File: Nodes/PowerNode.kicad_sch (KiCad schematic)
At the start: 12 parts, among them T1 Conn_01x01, U1 STM32G431KBT6, Y1 SG-8018CE_8.0000M-TJHPA3

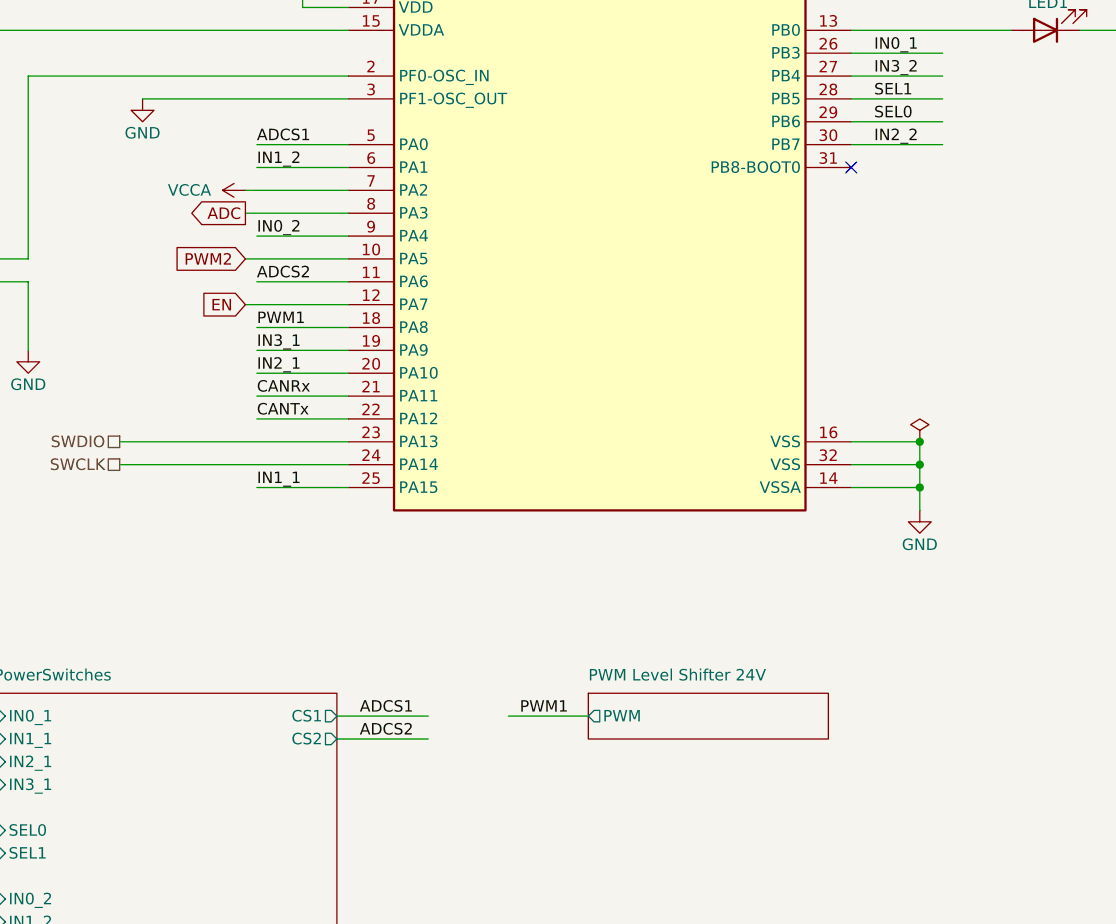
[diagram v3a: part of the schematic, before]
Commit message: Nodes v2.2.3
- Added one more PWM Level shifter
- Controllable amplitude of PWM by switches
- Added labels
- Added resistors to solve BOOT issue
- I2C1 pins changed
- More GND vias
- Higher resistance for adjustable voltage regulators
- Other small changes
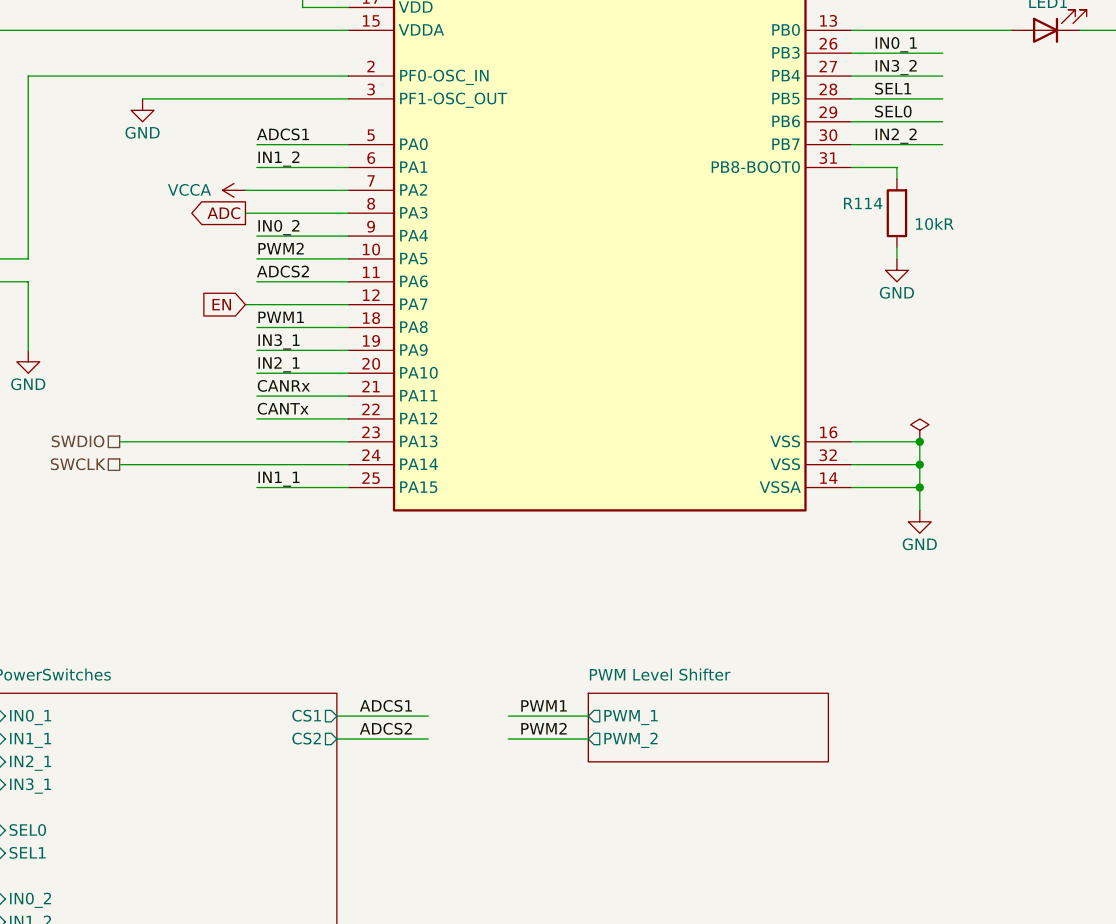
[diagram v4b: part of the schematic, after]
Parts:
- added R114: 10kR, Resistor_SMD:R_0805_2012Metric_Pad1.20x1.40mm_HandSolder, symbol Device:R
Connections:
- net GND: now also R114.1
- net at U1.31 (PB8-BOOT0): now also R114.2
- no-connect marks 2 -> 1
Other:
- sheet PWM Level Shifter 24V renamed PWM Level Shifter
- sheet PWM Level Shifter: file PWM_24V.kicad_sch -> PWM.kicad_sch
- sheet PWM Level Shifter ports: added PWM_1, PWM_2; removed PWM
